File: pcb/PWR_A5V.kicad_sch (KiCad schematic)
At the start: 4 parts, among them IC6 LP2951-50DRG4

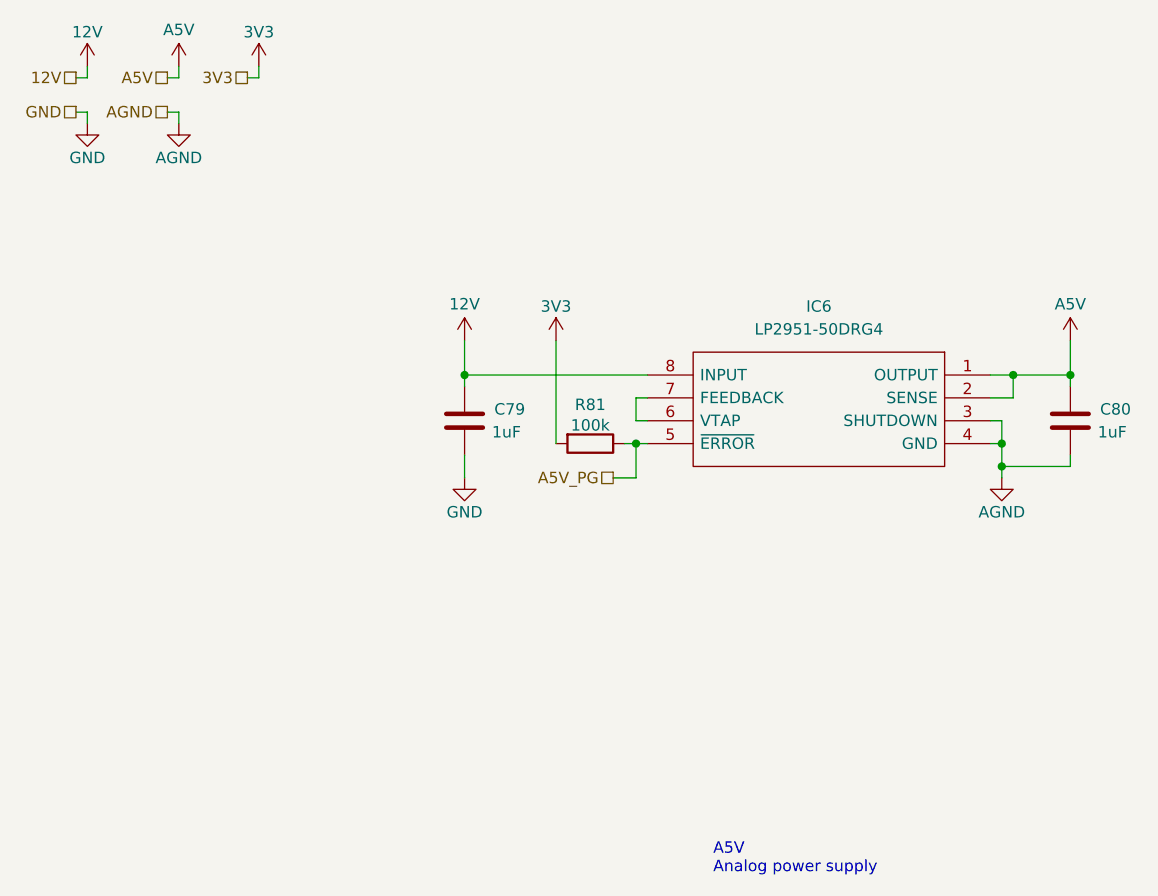
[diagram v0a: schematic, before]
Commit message: reannotated, updated some symbols
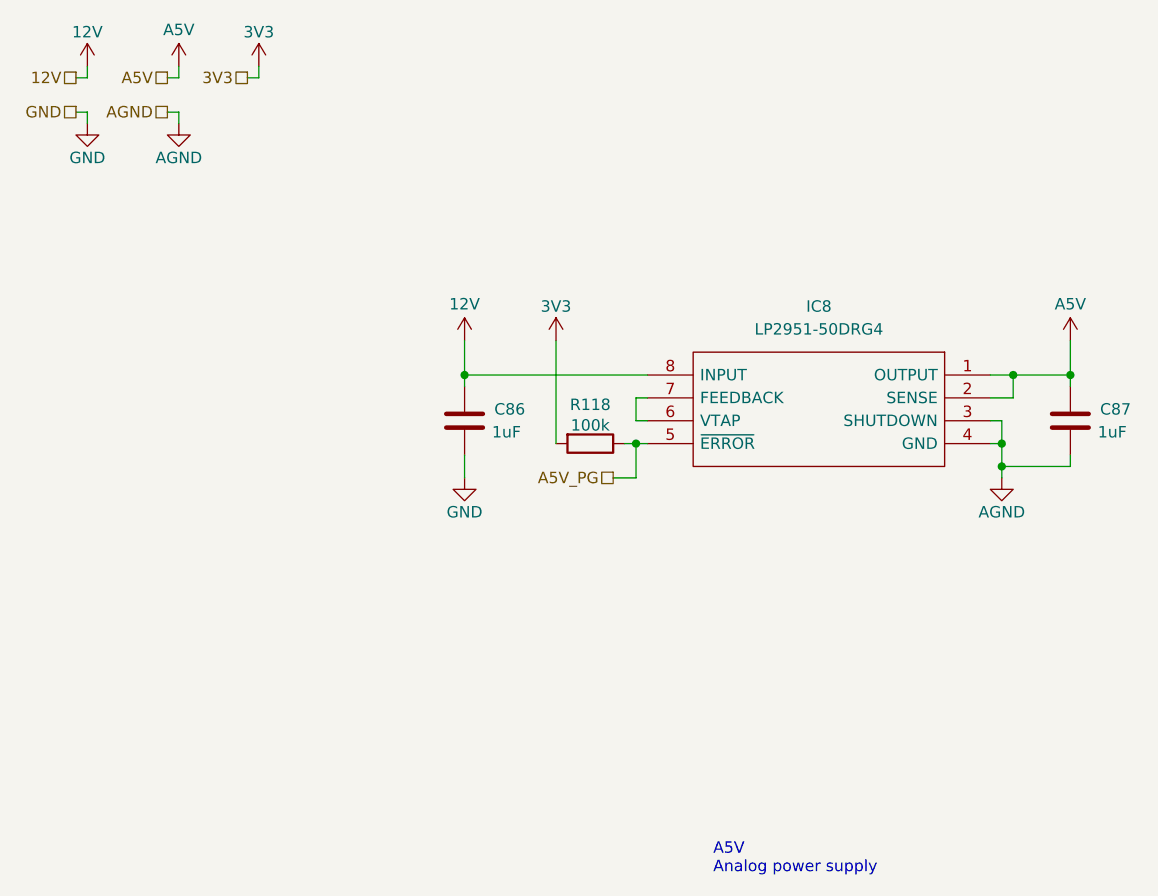
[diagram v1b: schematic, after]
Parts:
- renumbered C79 to C86, C80 to C87, IC6 to IC8, R81 to R118
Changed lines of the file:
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@@
 		(on_board yes)
 		(dnp no)
-		(property "Reference" "IC6"
+		(property "Reference" "IC8"
 			(at 102.87 45.72 0)
 			(effects
@@
 			(project "NCU"
 				(path "/3aee14c3-5480-4f7c-989e-3fef81779034/05e3be97-98f6-4518-a1a7-240d4da327e6/bd2125f3-b038-4fbf-8844-7722167ed0b9"
-					(reference "IC6")
+					(reference "IC8")
 					(unit 1)
 				)
@@
 		(on_board yes)
 		(dnp no)
-		(property "Reference" "#PWR0284"
+		(property "Reference" "#PWR0380"
 			(at 21.59 22.86 0)
 			(effects
@@
 			(project "NCU"
 				(path "/3aee14c3-5480-4f7c-989e-3fef81779034/05e3be97-98f6-4518-a1a7-240d4da327e6/bd2125f3-b038-4fbf-8844-7722167ed0b9"
-					(reference "#PWR0284")
+					(reference "#PWR0380")
 					(unit 1)
 				)
@@
 		(on_board yes)
 		(dnp no)
-		(property "Reference" "#PWR0289"
+		(property "Reference" "#PWR0385"
 			(at 63.5 53.34 0)
 			(effects
@@
 			(project "NCU"
 				(path "/3aee14c3-5480-4f7c-989e-3fef81779034/05e3be97-98f6-4518-a1a7-240d4da327e6/bd2125f3-b038-4fbf-8844-7722167ed0b9"
-					(reference "#PWR0289")
+					(reference "#PWR0385")
 					(unit 1)
 				)
@@
 		(on_board yes)
 		(dnp no)
-		(property "Reference" "#PWR0291"
+		(property "Reference" "#PWR0387"
 			(at 73.66 53.34 0)
 			(effects
@@
 			(project "NCU"
 				(path "/3aee14c3-5480-4f7c-989e-3fef81779034/05e3be97-98f6-4518-a1a7-240d4da327e6/bd2125f3-b038-4fbf-8844-7722167ed0b9"
-					(reference "#PWR0291")
+					(reference "#PWR0387")
 					(unit 1)
 				)
@@
 		(on_board yes)
 		(dnp no)
-		(property "Reference" "C80"
+		(property "Reference" "C87"
 			(at 134.112 57.15 0)
 			(effects
@@
 			(project "NCU"
 				(path "/3aee14c3-5480-4f7c-989e-3fef81779034/05e3be97-98f6-4518-a1a7-240d4da327e6/bd2125f3-b038-4fbf-8844-7722167ed0b9"
-					(reference "C80")
+					(reference "C87")
 					(unit 1)
 				)
@@
 		(on_board yes)
 		(dnp no)
-		(property "Reference" "R81"
+		(property "Reference" "R118"
 			(at 77.47 56.642 90)
 			(effects
@@
 			(project "NCU"
 				(path "/3aee14c3-5480-4f7c-989e-3fef81779034/05e3be97-98f6-4518-a1a7-240d4da327e6/bd2125f3-b038-4fbf-8844-7722167ed0b9"
-					(reference "R81")
+					(reference "R118")
 					(unit 1)
 				)
@@
 		(on_board yes)
 		(dnp no)
-		(property "Reference" "#PWR0287"
+		(property "Reference" "#PWR0383"
 			(at 31.75 31.75 0)
 			(effects
@@
 			(project "NCU"
 				(path "/3aee14c3-5480-4f7c-989e-3fef81779034/05e3be97-98f6-4518-a1a7-240d4da327e6/bd2125f3-b038-4fbf-8844-7722167ed0b9"
-					(reference "#PWR0287")
+					(reference "#PWR0383")
 					(unit 1)
 				)
@@
 		(on_board yes)
 		(dnp no)
-		(property "Reference" "#PWR0290"
+		(property "Reference" "#PWR0386"
 			(at 63.5 71.12 0)
 			(effects
@@
 			(project "NCU"
 				(path "/3aee14c3-5480-4f7c-989e-3fef81779034/05e3be97-98f6-4518-a1a7-240d4da327e6/bd2125f3-b038-4fbf-8844-7722167ed0b9"
-					(reference "#PWR0290")
+					(reference "#PWR0386")
 					(unit 1)
 				)
@@
 		(on_board yes)
 		(dnp no)
-		(property "Reference" "#PWR0292"
+		(property "Reference" "#PWR0388"
 			(at 123.19 71.12 0)
 			(effects
@@
 			(project "NCU"
 				(path "/3aee14c3-5480-4f7c-989e-3fef81779034/05e3be97-98f6-4518-a1a7-240d4da327e6/bd2125f3-b038-4fbf-8844-7722167ed0b9"
-					(reference "#PWR0292")
+					(reference "#PWR0388")
 					(unit 1)
 				)
@@
 		(on_board yes)
 		(dnp no)
-		(property "Reference" "#PWR0288"
+		(property "Reference" "#PWR0384"
 			(at 40.64 22.86 0)
 			(effects
@@
 			(project "NCU"
 				(path "/3aee14c3-5480-4f7c-989e-3fef81779034/05e3be97-98f6-4518-a1a7-240d4da327e6/bd2125f3-b038-4fbf-8844-7722167ed0b9"
-					(reference "#PWR0288")
+					(reference "#PWR0384")
 					(unit 1)
 				)
@@
 		(on_board yes)
 		(dnp no)
-		(property "Reference" "#PWR0286"
+		(property "Reference" "#PWR0382"
 			(at 31.75 22.86 0)
 			(effects
@@
 			(project "NCU"
 				(path "/3aee14c3-5480-4f7c-989e-3fef81779034/05e3be97-98f6-4518-a1a7-240d4da327e6/bd2125f3-b038-4fbf-8844-7722167ed0b9"
-					(reference "#PWR0286")
+					(reference "#PWR0382")
 					(unit 1)
 				)
@@
 		(on_board yes)
 		(dnp no)
-		(property "Reference" "#PWR0285"
+		(property "Reference" "#PWR0381"
 			(at 21.59 31.75 0)
 			(effects
@@
 			(project "NCU"
 				(path "/3aee14c3-5480-4f7c-989e-3fef81779034/05e3be97-98f6-4518-a1a7-240d4da327e6/bd2125f3-b038-4fbf-8844-7722167ed0b9"
-					(reference "#PWR0285")
+					(reference "#PWR0381")
 					(unit 1)
 				)
@@
 		(on_board yes)
 		(dnp no)
-		(property "Reference" "#PWR0293"
+		(property "Reference" "#PWR0389"
 			(at 130.81 53.34 0)
 			(effects
@@
 			(project "NCU"
 				(path "/3aee14c3-5480-4f7c-989e-3fef81779034/05e3be97-98f6-4518-a1a7-240d4da327e6/bd2125f3-b038-4fbf-8844-7722167ed0b9"
-					(reference "#PWR0293")
+					(reference "#PWR0389")
 					(unit 1)
 				)
@@
 		(on_board yes)
 		(dnp no)
-		(property "Reference" "C79"
+		(property "Reference" "C86"
 			(at 66.802 57.15 0)
 			(effects
@@
 			(project "NCU"
 				(path "/3aee14c3-5480-4f7c-989e-3fef81779034/05e3be97-98f6-4518-a1a7-240d4da327e6/bd2125f3-b038-4fbf-8844-7722167ed0b9"
-					(reference "C79")
-					(unit 1)
-				)
+					(reference "C86")
+					(unit 1)
+				)

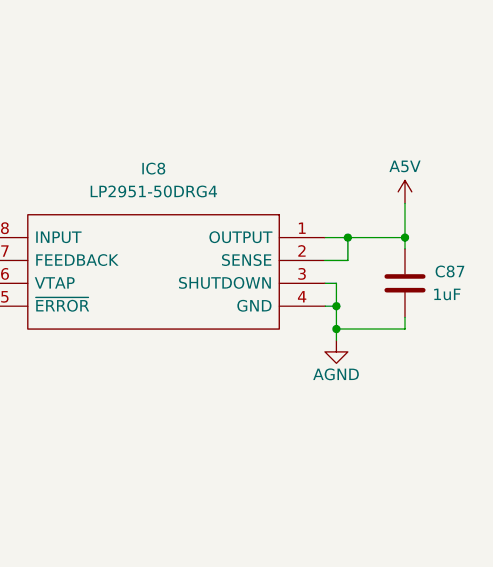
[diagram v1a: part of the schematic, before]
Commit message: all power supplies laid out I think
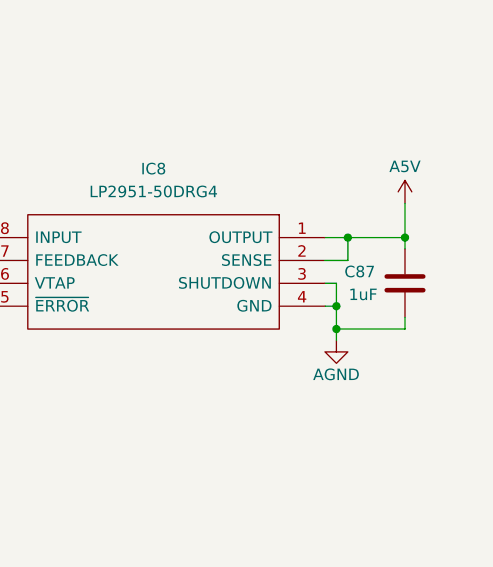
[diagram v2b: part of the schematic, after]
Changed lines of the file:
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@@
 		(lib_id "Device:C")
 		(at 130.81 58.42 0)
+		(mirror y)
 		(unit 1)
 		(exclude_from_sim no)
@@
 		(dnp no)
 		(property "Reference" "C87"
-			(at 134.112 57.15 0)
+			(at 127.508 57.15 0)
 			(effects
 				(font
@@
 		)
 		(property "Value" "1uF"
-			(at 133.858 59.69 0)
+			(at 127.762 59.69 0)
 			(effects
 				(font
@@
 		)
 		(property "Footprint" "Capacitor_SMD:C_0603_1608Metric_Pad1.08x0.95mm_HandSolder"
-			(at 131.7752 62.23 0)
+			(at 129.8448 62.23 0)
 			(effects
 				(font

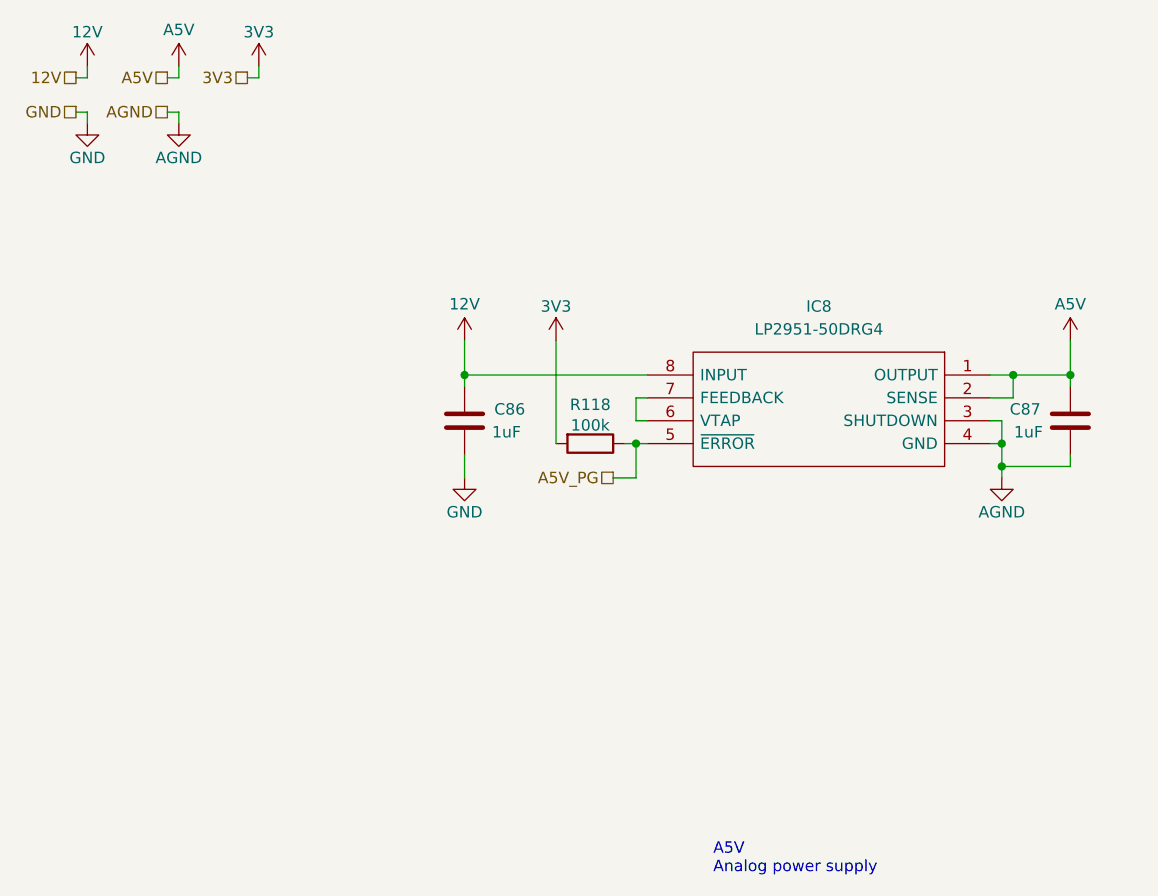
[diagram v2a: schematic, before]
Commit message: removed AGND and added ground garden
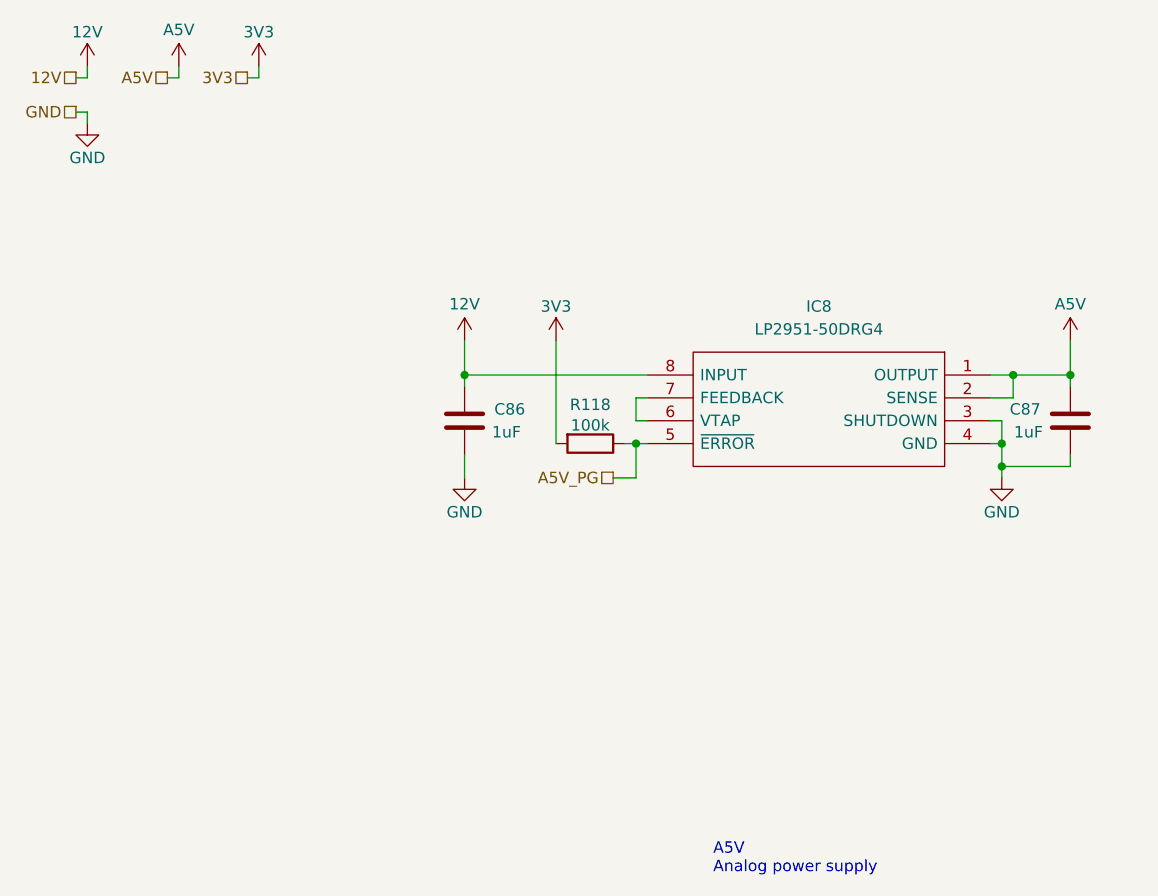
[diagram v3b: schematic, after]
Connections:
- net AGND is gone; now on net GND: C87.2, IC8.3 (SHUTDOWN), IC8.4 (GND)
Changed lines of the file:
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@@
-	(wire
-		(pts
-			(xy 31.75 24.13) (xy 31.75 25.4)
-		)
-		(stroke
-			(width 0)
-			(type default)
-		)
-	)
 	(wire
 		(pts
@@
 	(wire
 		(pts
-			(xy 31.75 24.13) (xy 30.48 24.13)
-		)
-		(stroke
-			(width 0)
-			(type default)
-		)
-	)
-	(wire
-		(pts
 			(xy 31.75 20.32) (xy 31.75 19.05)
 		)
@@
 			(width 0)
 			(type default)
-		)
-	)
-	(hierarchical_label "AGND"
-		(shape passive)
-		(at 30.48 24.13 180)
-		(effects
-			(font
-				(size 1.27 1.27)
-			)
-			(justify right)
 		)
 	)
@@
 	(symbol
 		(lib_id "power:GND")
-		(at 31.75 25.4 0)
-		(unit 1)
-		(exclude_from_sim no)
-		(in_bom yes)
-		(on_board yes)
-		(dnp no)
-		(property "Reference" "#PWR0383"
-			(at 31.75 31.75 0)
-			(effects
-				(font
-					(size 1.27 1.27)
-				)
-				(hide yes)
-			)
-		)
-		(property "Value" "AGND"
-			(at 31.75 29.21 0)
-			(effects
-				(font
-					(size 1.27 1.27)
-				)
-			)
-		)
-		(property "Footprint" ""
-			(at 31.75 25.4 0)
-			(effects
-				(font
-					(size 1.27 1.27)
-				)
-				(hide yes)
-			)
-		)
-		(property "Datasheet" ""
-			(at 31.75 25.4 0)
-			(effects
-				(font
-					(size 1.27 1.27)
-				)
-				(hide yes)
-			)
-		)
-		(property "Description" "Power symbol creates a global label with name \"GND\" , ground"
-			(at 31.75 25.4 0)
-			(effects
-				(font
-					(size 1.27 1.27)
-				)
-				(hide yes)
-			)
-		)
-		(pin "1"
-		)
-		(instances
-			(project "NCU"
-				(path "/3aee14c3-5480-4f7c-989e-3fef81779034/05e3be97-98f6-4518-a1a7-240d4da327e6/bd2125f3-b038-4fbf-8844-7722167ed0b9"
-					(reference "#PWR0383")
-					(unit 1)
-				)
-			)
-		)
-	)
-	(symbol
-		(lib_id "power:GND")
 		(at 63.5 64.77 0)
 		(unit 1)
@@
 			)
 		)
-		(property "Value" "AGND"
+		(property "Value" "GND"
 			(at 123.19 68.58 0)
 			(effects

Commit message: updates from bom release
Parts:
- C86, C87: value 1uF -> 1u
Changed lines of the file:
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@@
 			)
 		)
-		(property "Value" "1uF"
+		(property "Value" "1u"
 			(at 127.762 59.69 0)
 			(effects
@@
 			)
 		)
-		(property "Value" "1uF"
+		(property "Value" "1u"
 			(at 66.548 59.69 0)
 			(effects
